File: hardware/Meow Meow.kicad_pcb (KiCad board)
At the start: 2 copper layers, 98.7 x 61 mm, 38 parts, among them P1 D, P10 A, P11 W, P12 MOUSE_LEFT, P13 CONN_01X06, P14 CONN_01X06, P2 SPACE, P3 KEY_RIGHT_ARROW, P4 SWD, P5 KEY_LEFT_ARROW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

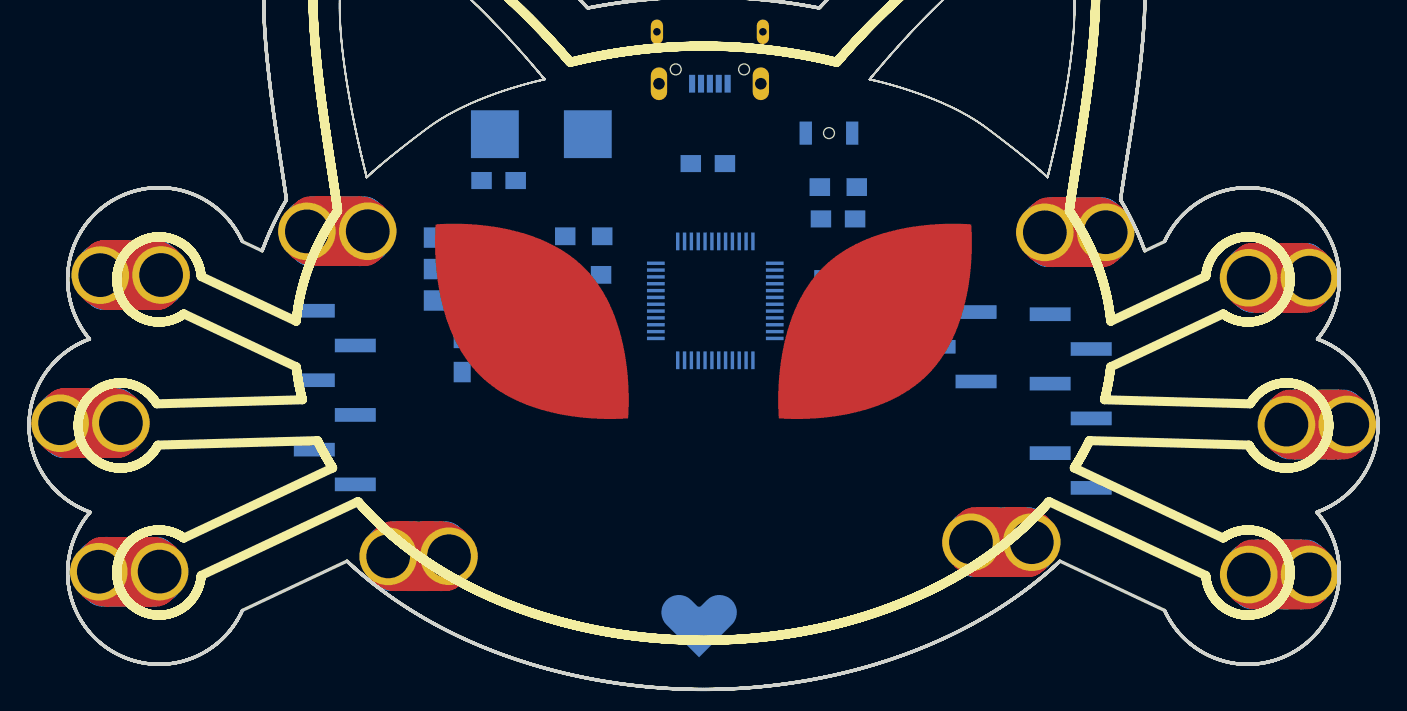
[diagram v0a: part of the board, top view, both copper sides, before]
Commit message: place components to route
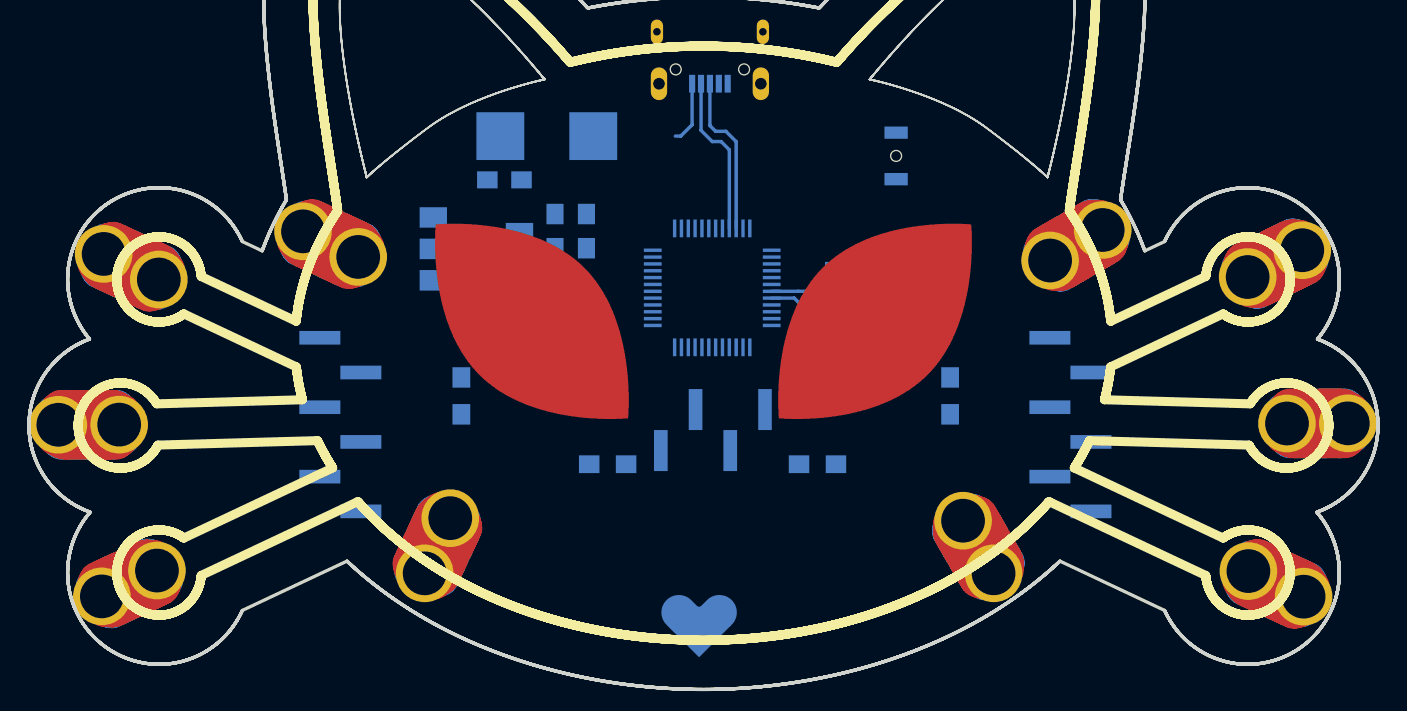
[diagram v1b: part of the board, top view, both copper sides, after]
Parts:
- moved P11 87.6 mm to (187.6, 121.1)
- moved P5 84.1 mm to (100.7, 132.7), turned to 115 degrees
- moved P3 69.4 mm to (115.4, 108.0), turned to 65 degrees
- moved P7 68.9 mm to (184.5, 109.3), turned to 116 degrees
- moved P10 53.0 mm to (169.7, 108.0), turned to 300 degrees
- moved P8 41.0 mm to (123.2, 129.8), turned to 155 degrees
- moved P6 29.9 mm to (184.6, 132.8), turned to 65 degrees
- moved P1 26.5 mm to (162.7, 130.2), turned to 30 degrees
- moved P4 19.2 mm to (143.2, 121.5), turned to 180 degrees
- moved C2 15.8 mm to (153.4, 113.8), turned to 0 degrees
- moved svg2mod 15.4 mm to (126.5, 119.0)
- moved D1 14.7 mm to (124.8, 119.0), turned to 90 degrees
- moved R2 14.0 mm to (135.6, 124.0)
- moved P2 11.8 mm to (100.8, 109.7), turned to 65 degrees
- moved D2 11.6 mm to (160.6, 119.0), turned to 90 degrees
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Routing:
- net /D-: track 0.00 -> 11.8 mm
- net /D+: track 0.00 -> 11.8 mm
- net +3V3: track 0.00 -> 5.39 mm
- net Net-(C1-Pad1): track 0.00 -> 4.81 mm
- net Net-(F1-Pad2): track 0.00 -> 4.57 mm
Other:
- net class Default: trace_width 0.5 -> 0.25

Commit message: Start routing
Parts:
- moved P1 39.8 mm to (122.9, 130.3), turned to 155 degrees
- moved P8 39.5 mm to (162.7, 130.2), turned to 30 degrees
- moved P11 22.2 mm to (169.7, 108.0), turned to 300 degrees
- moved P3 21.9 mm to (97.8, 121.1), turned to 90 degrees
- moved P12 21.9 mm to (115.5, 108.2), turned to 65 degrees
- moved P10 14.9 mm to (184.6, 109.3), turned to 117 degrees
- moved P7 12.2 mm to (187.6, 121.1), turned to 90 degrees
- turned P5 to 295 degrees
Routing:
- net +3V3: track 5.39 -> 99.8 mm, vias 0 -> 5
- net /Y2: track 0.00 -> 66.3 mm
- net /Y3: track 0.00 -> 66.0 mm
- net /Y0: track 0.00 -> 65.4 mm
- net /Y1: track 0.00 -> 62.7 mm
- net /I2S_SCK: track 0.00 -> 58.2 mm, vias 0 -> 2
- net /Y4: track 0.00 -> 57.2 mm
- net /Y9: track 0.00 -> 54.7 mm
- net /CS: track 0.00 -> 47.9 mm, vias 0 -> 2
- net /I2S_D1/X7: track 0.00 -> 42.6 mm, vias 0 -> 2
- net /Y5: track 0.00 -> 39.3 mm
- net GND: track 0.00 -> 37.4 mm, vias 0 -> 8
- net /Y15: track 0.00 -> 35.6 mm
- net /D8: track 0.00 -> 31.9 mm, vias 0 -> 2
- net /SWDIO: track 0.00 -> 24.3 mm, vias 0 -> 2
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- added copper zone on B.Cu, net GND
- added copper zone on F.Cu, net GND
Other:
- net class Default: trace_width 0.25 -> 0.35; via_dia 1.4 -> 0.6; via_drill 0.8 -> 0.4
- net class vcc added: clearance 0.2, trace_width 0.5, via_dia 1.4, via_drill 0.8

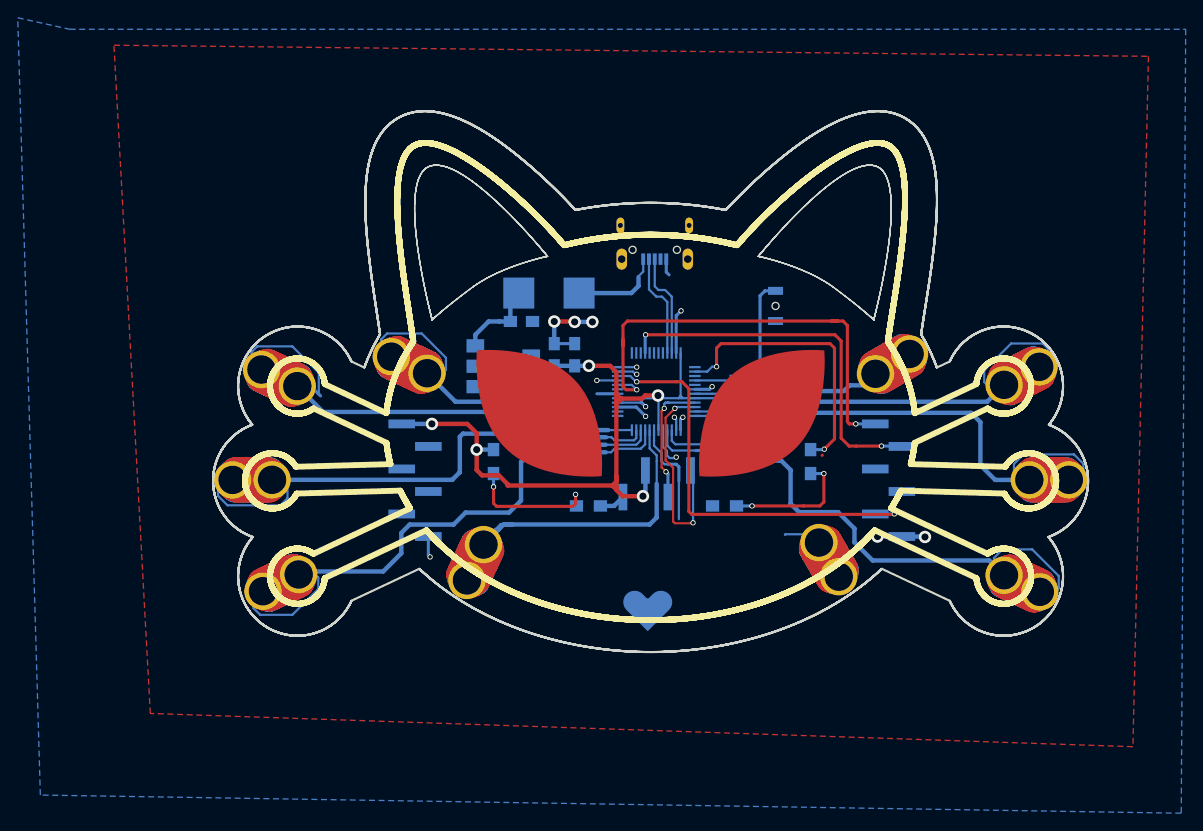
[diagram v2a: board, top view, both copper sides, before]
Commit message: Change eyes to Silks
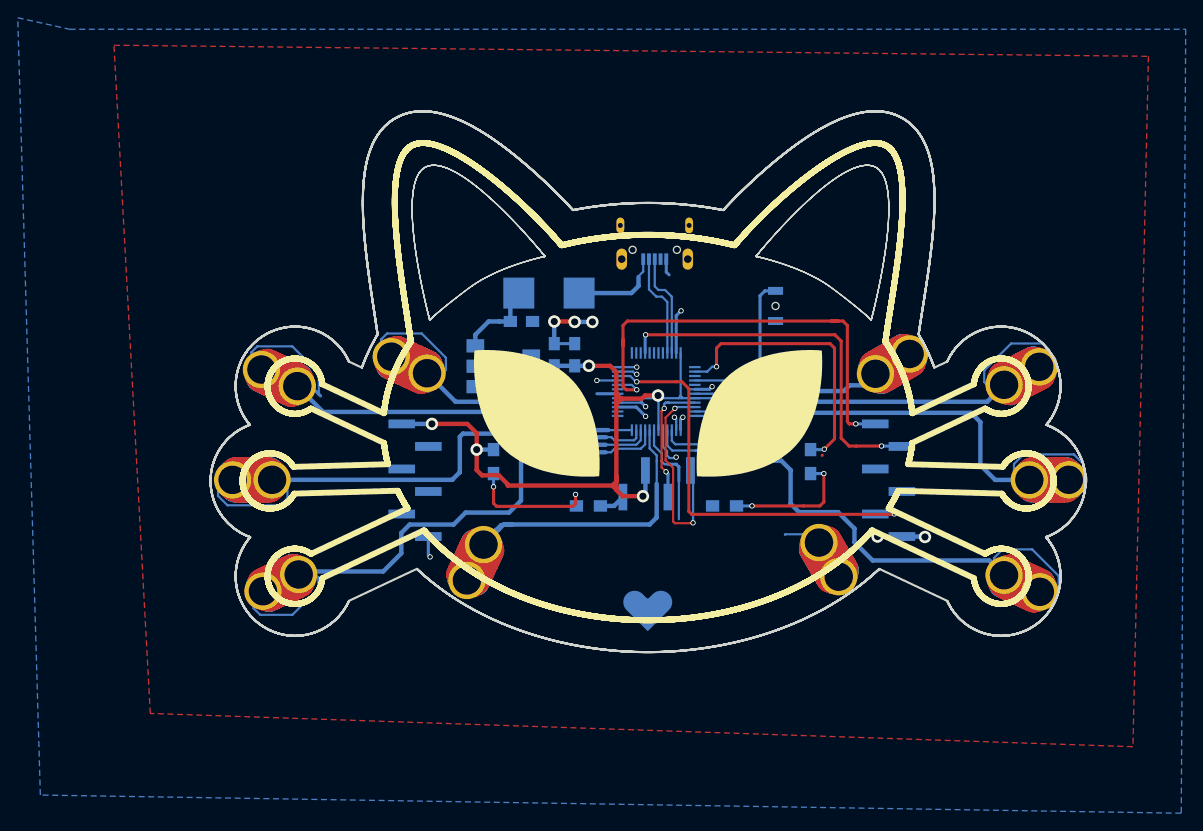
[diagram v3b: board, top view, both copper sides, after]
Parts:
- moved svg2mod 0.28 mm to (142.2, 109.3)
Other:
- outline, holes or cut-outs redrawn
